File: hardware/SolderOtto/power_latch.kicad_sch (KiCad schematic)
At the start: 1 part, among them U501 SN74LVC2G125

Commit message: save wip
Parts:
- renumbered U501 to U601
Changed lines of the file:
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@@
 		(dnp no)
 		(fields_autoplaced yes)
-		(property "Reference" "#PWR0501"
+		(property "Reference" "#PWR0616"
 			(at 92.71 96.52 0)
 			(effects
@@
 		(instances
 			(project "SolderOtto"
-				(path "/04e99464-bf33-4a4f-8397-d26b5ec904f3/1be905ad-e645-4d96-915b-9416f5f3d20b"
-					(reference "#PWR0501")
+				(path "/04e99464-bf33-4a4f-8397-d26b5ec904f3/57a4c2b0-a7ab-4dc9-9bcc-6bd7e1b882d1/38c12336-e051-4519-b2f1-090dafa1bb9e"
+					(reference "#PWR0616")
 					(unit 1)
 				)
@@
 		(dnp no)
 		(fields_autoplaced yes)
-		(property "Reference" "U501"
+		(property "Reference" "U601"
 			(at 151.13 86.36 0)
 			(effects
@@
 		(instances
 			(project "SolderOtto"
-				(path "/04e99464-bf33-4a4f-8397-d26b5ec904f3/1be905ad-e645-4d96-915b-9416f5f3d20b"
-					(reference "U501")
+				(path "/04e99464-bf33-4a4f-8397-d26b5ec904f3/57a4c2b0-a7ab-4dc9-9bcc-6bd7e1b882d1/38c12336-e051-4519-b2f1-090dafa1bb9e"
+					(reference "U601")
 					(unit 1)
 				)
@@
 		(dnp no)
 		(fields_autoplaced yes)
-		(property "Reference" "#PWR0502"
+		(property "Reference" "#PWR0617"
 			(at 92.71 119.38 0)
 			(effects
@@
 		(instances
 			(project "SolderOtto"
-				(path "/04e99464-bf33-4a4f-8397-d26b5ec904f3/1be905ad-e645-4d96-915b-9416f5f3d20b"
-					(reference "#PWR0502")
+				(path "/04e99464-bf33-4a4f-8397-d26b5ec904f3/57a4c2b0-a7ab-4dc9-9bcc-6bd7e1b882d1/38c12336-e051-4519-b2f1-090dafa1bb9e"
+					(reference "#PWR0617")
 					(unit 1)
 				)
@@
 		(dnp no)
 		(fields_autoplaced yes)
-		(property "Reference" "U501"
+		(property "Reference" "U601"
 			(at 96.52 101.5999 0)
 			(effects
@@
 		(instances
 			(project "SolderOtto"
-				(path "/04e99464-bf33-4a4f-8397-d26b5ec904f3/1be905ad-e645-4d96-915b-9416f5f3d20b"
-					(reference "U501")
+				(path "/04e99464-bf33-4a4f-8397-d26b5ec904f3/57a4c2b0-a7ab-4dc9-9bcc-6bd7e1b882d1/38c12336-e051-4519-b2f1-090dafa1bb9e"
+					(reference "U601")
 					(unit 3)
 				)
@@
 		(on_board yes)
 		(dnp no)
-		(property "Reference" "#FLG0502"
+		(property "Reference" "#FLG0602"
 			(at 166.37 112.395 0)
 			(effects
@@
 		(instances
 			(project "SolderOtto"
-				(path "/04e99464-bf33-4a4f-8397-d26b5ec904f3/1be905ad-e645-4d96-915b-9416f5f3d20b"
-					(reference "#FLG0502")
+				(path "/04e99464-bf33-4a4f-8397-d26b5ec904f3/57a4c2b0-a7ab-4dc9-9bcc-6bd7e1b882d1/38c12336-e051-4519-b2f1-090dafa1bb9e"
+					(reference "#FLG0602")
 					(unit 1)
 				)
@@
 		(dnp no)
 		(fields_autoplaced yes)
-		(property "Reference" "U501"
+		(property "Reference" "U601"
 			(at 151.13 110.49 0)
 			(effects
@@
 		(instances
 			(project "SolderOtto"
-				(path "/04e99464-bf33-4a4f-8397-d26b5ec904f3/1be905ad-e645-4d96-915b-9416f5f3d20b"
-					(reference "U501")
+				(path "/04e99464-bf33-4a4f-8397-d26b5ec904f3/57a4c2b0-a7ab-4dc9-9bcc-6bd7e1b882d1/38c12336-e051-4519-b2f1-090dafa1bb9e"
+					(reference "U601")
 					(unit 2)
 				)
@@
 		(on_board yes)
 		(dnp no)
-		(property "Reference" "#FLG0501"
+		(property "Reference" "#FLG0601"
 			(at 166.37 88.265 0)
 			(effects
@@
 		(instances
 			(project "SolderOtto"
-				(path "/04e99464-bf33-4a4f-8397-d26b5ec904f3/1be905ad-e645-4d96-915b-9416f5f3d20b"
-					(reference "#FLG0501")
+				(path "/04e99464-bf33-4a4f-8397-d26b5ec904f3/57a4c2b0-a7ab-4dc9-9bcc-6bd7e1b882d1/38c12336-e051-4519-b2f1-090dafa1bb9e"
+					(reference "#FLG0601")
 					(unit 1)
 				)

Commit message: wip
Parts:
- removed U601: SN74LVC2G125, Package_SO:VSSOP-8_2.3x2mm_P0.5mm, symbol mylib_ic:SN74LVC2G125

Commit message: update schematic
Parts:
- added U706: SN74LVC125A, Package_SO:TSSOP-14_4.4x5mm_P0.65mm, symbol mylib_ic:SN74LVC125A
- added U707: TS5A3159ADCK, Package_TO_SOT_SMD:SOT-363_SC-70-6, symbol Analog_Switch:TS5A3159ADCK
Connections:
- new net +3V3: U706.14 (V_{CC}), U707.4, U707.5 (V+)
- new net GND: U706.7 (GND), U707.2 (GND)
- new net IN_COM: U706.2 (A)
- new net IN_LOAD0: U706.5 (A)
- new net IN_LOAD1: U706.9 (A)
- new net LOW_SIDE: U707.6
- new net OUT_COM_H: U706.3 (Y)
- new net OUT_COM_L: U706.1 (~{OE}), U707.3
- new net OUT_LOAD0_H: U706.6 (Y)
- new net OUT_LOAD1_H: U706.8 (Y)
- new net OUT_LOAD_L: U706.10 (~{OE}), U706.4 (~{OE}), U707.1
- no-connect marks 0 -> 3

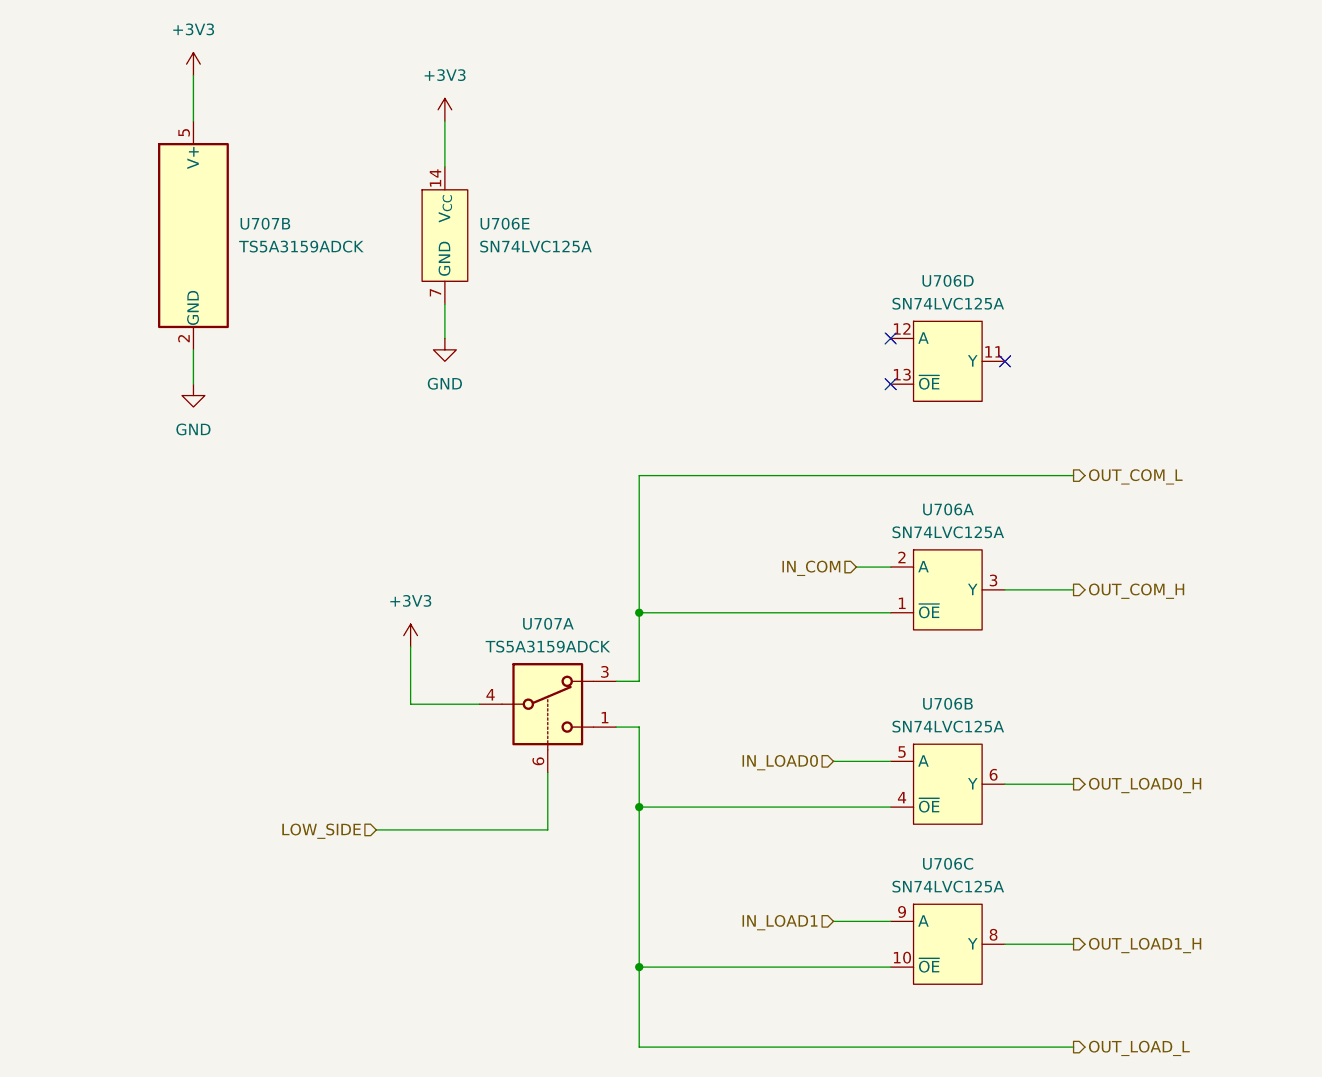
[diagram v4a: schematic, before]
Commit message: create adapter to enclosure for display
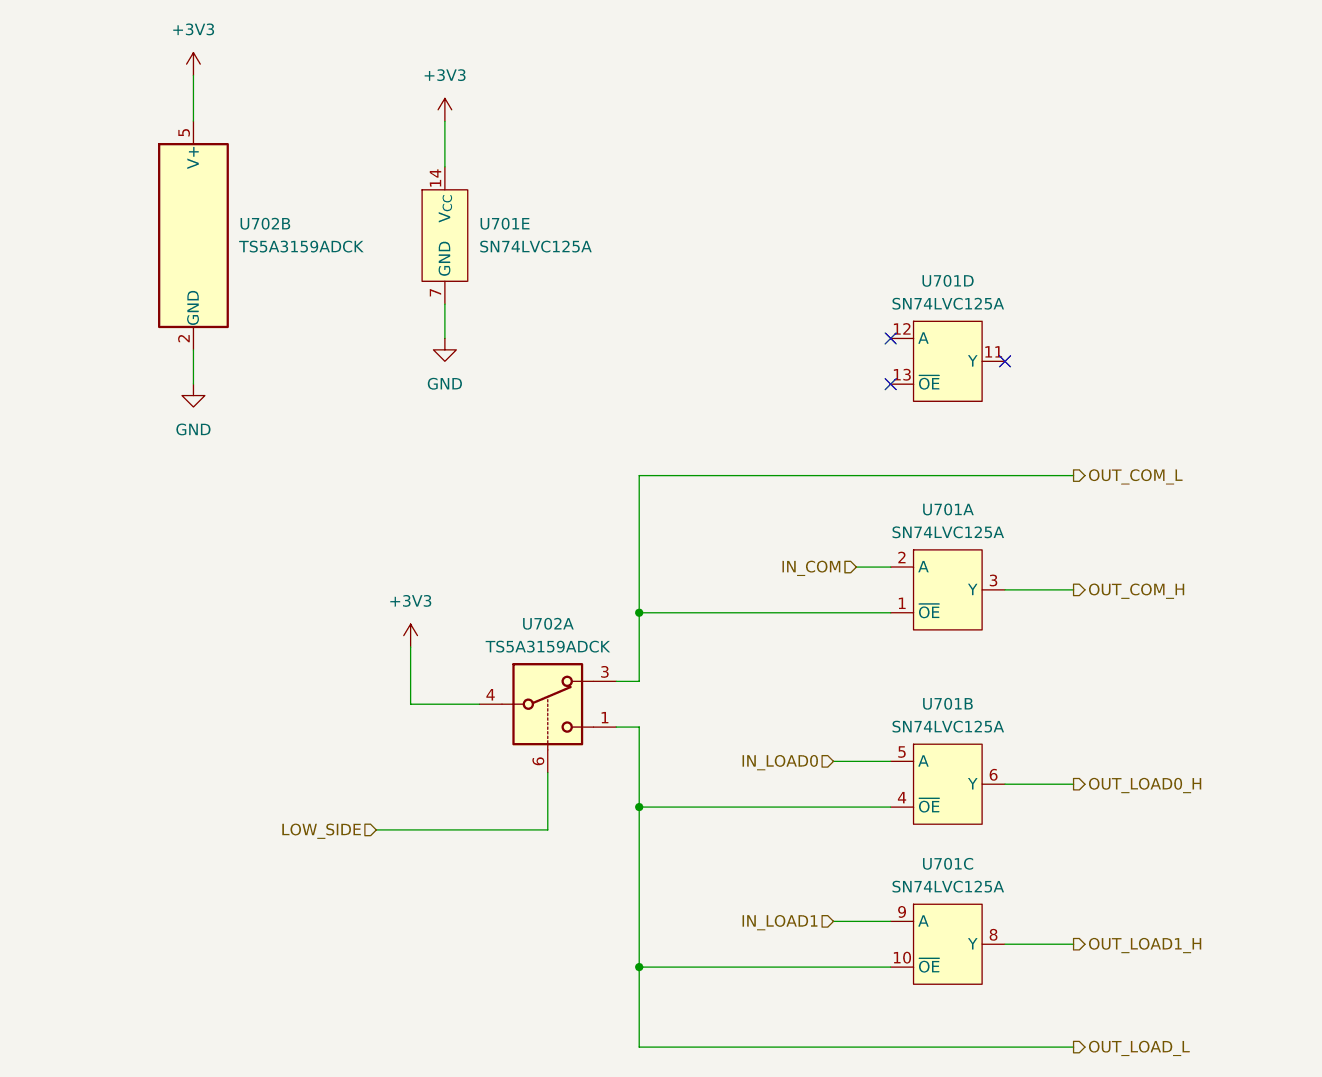
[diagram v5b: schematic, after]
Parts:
- renumbered U706 to U701, U707 to U702
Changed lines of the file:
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@@
 		(dnp no)
 		(fields_autoplaced yes)
-		(property "Reference" "#PWR0744"
+		(property "Reference" "#PWR0704"
 			(at 66.04 63.5 0)
 			(effects
@@
 			(project ""
 				(path "/04e99464-bf33-4a4f-8397-d26b5ec904f3/57a4c2b0-a7ab-4dc9-9bcc-6bd7e1b882d1/38c12336-e051-4519-b2f1-090dafa1bb9e"
-					(reference "#PWR0744")
+					(reference "#PWR0704")
 					(unit 1)
 				)
@@
 		(dnp no)
 		(fields_autoplaced yes)
-		(property "Reference" "#PWR0743"
+		(property "Reference" "#PWR0705"
 			(at 90.17 90.17 0)
 			(effects
@@
 			(project ""
 				(path "/04e99464-bf33-4a4f-8397-d26b5ec904f3/57a4c2b0-a7ab-4dc9-9bcc-6bd7e1b882d1/38c12336-e051-4519-b2f1-090dafa1bb9e"
-					(reference "#PWR0743")
+					(reference "#PWR0705")
 					(unit 1)
 				)
@@
 		(dnp no)
 		(fields_autoplaced yes)
-		(property "Reference" "U706"
+		(property "Reference" "U701"
 			(at 149.86 92.71 0)
 			(effects
@@
 			(project ""
 				(path "/04e99464-bf33-4a4f-8397-d26b5ec904f3/57a4c2b0-a7ab-4dc9-9bcc-6bd7e1b882d1/38c12336-e051-4519-b2f1-090dafa1bb9e"
-					(reference "U706")
+					(reference "U701")
 					(unit 2)
 				)
@@
 		(dnp no)
 		(fields_autoplaced yes)
-		(property "Reference" "#PWR0745"
+		(property "Reference" "#PWR0703"
 			(at 93.98 58.42 0)
 			(effects
@@
 			(project "SolderOtto"
 				(path "/04e99464-bf33-4a4f-8397-d26b5ec904f3/57a4c2b0-a7ab-4dc9-9bcc-6bd7e1b882d1/38c12336-e051-4519-b2f1-090dafa1bb9e"
-					(reference "#PWR0745")
+					(reference "#PWR0703")
 					(unit 1)
 				)
@@
 		(dnp no)
 		(fields_autoplaced yes)
-		(property "Reference" "U706"
+		(property "Reference" "U701"
 			(at 149.86 45.72 0)
 			(effects
@@
 			(project ""
 				(path "/04e99464-bf33-4a4f-8397-d26b5ec904f3/57a4c2b0-a7ab-4dc9-9bcc-6bd7e1b882d1/38c12336-e051-4519-b2f1-090dafa1bb9e"
-					(reference "U706")
+					(reference "U701")
 					(unit 4)
 				)
@@
 		(dnp no)
 		(fields_autoplaced yes)
-		(property "Reference" "U706"
+		(property "Reference" "U701"
 			(at 149.86 110.49 0)
 			(effects
@@
 			(project ""
 				(path "/04e99464-bf33-4a4f-8397-d26b5ec904f3/57a4c2b0-a7ab-4dc9-9bcc-6bd7e1b882d1/38c12336-e051-4519-b2f1-090dafa1bb9e"
-					(reference "U706")
+					(reference "U701")
 					(unit 3)
 				)
@@
 		(dnp no)
 		(fields_autoplaced yes)
-		(property "Reference" "U707"
+		(property "Reference" "U702"
 			(at 105.41 83.82 0)
 			(effects
@@
 			(project ""
 				(path "/04e99464-bf33-4a4f-8397-d26b5ec904f3/57a4c2b0-a7ab-4dc9-9bcc-6bd7e1b882d1/38c12336-e051-4519-b2f1-090dafa1bb9e"
-					(reference "U707")
+					(reference "U702")
 					(unit 1)
 				)
@@
 		(dnp no)
 		(fields_autoplaced yes)
-		(property "Reference" "U706"
+		(property "Reference" "U701"
 			(at 149.86 71.12 0)
 			(effects
@@
 			(project ""
 				(path "/04e99464-bf33-4a4f-8397-d26b5ec904f3/57a4c2b0-a7ab-4dc9-9bcc-6bd7e1b882d1/38c12336-e051-4519-b2f1-090dafa1bb9e"
-					(reference "U706")
+					(reference "U701")
 					(unit 1)
 				)
@@
 		(dnp no)
 		(fields_autoplaced yes)
-		(property "Reference" "U707"
+		(property "Reference" "U702"
 			(at 71.12 39.3699 0)
 			(effects
@@
 			(project ""
 				(path "/04e99464-bf33-4a4f-8397-d26b5ec904f3/57a4c2b0-a7ab-4dc9-9bcc-6bd7e1b882d1/38c12336-e051-4519-b2f1-090dafa1bb9e"
-					(reference "U707")
+					(reference "U702")
 					(unit 2)
 				)
@@
 		(dnp no)
 		(fields_autoplaced yes)
-		(property "Reference" "#PWR0746"
+		(property "Reference" "#PWR0702"
 			(at 93.98 31.75 0)
 			(effects
@@
 			(project "SolderOtto"
 				(path "/04e99464-bf33-4a4f-8397-d26b5ec904f3/57a4c2b0-a7ab-4dc9-9bcc-6bd7e1b882d1/38c12336-e051-4519-b2f1-090dafa1bb9e"
-					(reference "#PWR0746")
+					(reference "#PWR0702")
 					(unit 1)
 				)
@@
 		(dnp no)
 		(fields_autoplaced yes)
-		(property "Reference" "#PWR0747"
+		(property "Reference" "#PWR0701"
 			(at 66.04 26.67 0)
 			(effects
@@
 			(project "SolderOtto"
 				(path "/04e99464-bf33-4a4f-8397-d26b5ec904f3/57a4c2b0-a7ab-4dc9-9bcc-6bd7e1b882d1/38c12336-e051-4519-b2f1-090dafa1bb9e"
-					(reference "#PWR0747")
+					(reference "#PWR0701")
 					(unit 1)
 				)
@@
 		(dnp no)
 		(fields_autoplaced yes)
-		(property "Reference" "U706"
+		(property "Reference" "U701"
 			(at 97.79 39.3699 0)
 			(effects
@@
 			(project ""
 				(path "/04e99464-bf33-4a4f-8397-d26b5ec904f3/57a4c2b0-a7ab-4dc9-9bcc-6bd7e1b882d1/38c12336-e051-4519-b2f1-090dafa1bb9e"
-					(reference "U706")
+					(reference "U701")
 					(unit 5)
 				)

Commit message: layout finished
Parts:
- added C701, C702: 100n, Capacitor_SMD:C_0603_1608Metric, symbol Device:C
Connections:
- net +3V3: now also C701.1, C702.1
- net GND: now also C701.2, C702.2
- net IN_COM: now also U701.12 (A); no longer U701.2 (A)
- net OUT_COM_H: now also U701.11 (Y); no longer U701.3 (Y)
- net OUT_COM_L: now also U701.13 (~{OE}); no longer U701.1 (~{OE})
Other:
- moved on the sheet: U701A, U701D

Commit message: fix some part numbers
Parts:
- U701: Digikey (none) -> 296-1222-1-ND
- U702: Digikey (none) -> 296-21188-1-ND
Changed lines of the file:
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@@
+			)
+		)
+		(property "Digikey" "296-1222-1-ND"
+			(at 149.86 101.6 0)
+			(effects
+				(font
+					(size 1.27 1.27)
+				)
+				(hide yes)
 			)
 		)
@@
 			)
 		)
+		(property "Digikey" "296-1222-1-ND"
+			(at 149.86 80.01 0)
+			(effects
+				(font
+					(size 1.27 1.27)
+				)
+				(hide yes)
+			)
+		)
 		(pin "13"
 		)
@@
 			)
 		)
+		(property "Digikey" "296-1222-1-ND"
+			(at 149.86 119.38 0)
+			(effects
+				(font
+					(size 1.27 1.27)
+				)
+				(hide yes)
+			)
+		)
 		(pin "13"
 		)
@@
 		)
 		(property "Description" "Single SPDT Analog Switch, 1.65-V to 5.5-V Single-Supply Operation, 1Ohm Ron, SC-70-6"
+			(at 105.41 92.71 0)
+			(effects
+				(font
+					(size 1.27 1.27)
+				)
+				(hide yes)
+			)
+		)
+		(property "Digikey" "296-21188-1-ND"
 			(at 105.41 92.71 0)
 			(effects
@@
 			)
 		)
+		(property "Digikey" "296-1222-1-ND"
+			(at 149.86 54.61 0)
+			(effects
+				(font
+					(size 1.27 1.27)
+				)
+				(hide yes)
+			)
+		)
 		(pin "13"
 		)
@@
 			)
 		)
+		(property "Digikey" "296-21188-1-ND"
+			(at 66.04 40.64 0)
+			(effects
+				(font
+					(size 1.27 1.27)
+				)
+				(hide yes)
+			)
+		)
 		(pin "5"
 		)
@@
 			(at 93.98 39.37 0)
 			(effects
+				(font
+					(size 1.27 1.27)
+				)
+				(hide yes)
+			)
+		)
+		(property "Digikey" "296-1222-1-ND"
+			(at 93.98 39.37 0)
+			(effects
